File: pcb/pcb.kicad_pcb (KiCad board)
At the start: 2 copper layers, 168.9 x 103.7 mm, 129 parts, among them J1 MJ-4PP-9, J2 MJ-4PP-9, J3 USB_C_Receptacle_USB2.0_16P, J4 USB to TTL, J5 Conn_01x03, J6 Conn_01x03, SW1 KEY_SW, SW10 KEY_SW, SW11 KEY_SW, SW12 KEY_SW, SW13 KEY_SW, SW14 KEY_SW, SW15 KEY_SW, SW16 KEY_SW, SW17 KEY_SW, SW18 KEY_SW, SW19 KEY_SW, SW2 KEY_SW, SW20 KEY_SW, SW21 KEY_SW, SW22 KEY_SW, SW23 KEY_SW, SW24 KEY_SW, SW25 KEY_SW, SW26 KEY_SW, SW27 RotaryEncoder, SW3 KEY_SW, SW30 KEY_SW, SW31 KEY_SW, SW32 KEY_SW, SW33 KEY_SW, SW34 KEY_SW, SW35 KEY_SW, SW36 KEY_SW, SW37 KEY_SW, SW38 KEY_SW, SW39 KEY_SW, SW4 KEY_SW, SW40 KEY_SW, SW41 KEY_SW, SW42 KEY_SW, SW43 KEY_SW, SW44 KEY_SW, SW45 KEY_SW, SW46 KEY_SW, SW47 KEY_SW, SW48 KEY_SW, SW49 KEY_SW, SW5 KEY_SW, SW50 KEY_SW, SW51 KEY_SW, SW52 KEY_SW, SW53 KEY_SW, SW54 KEY_SW, SW6 KEY_SW, SW60 RESET_SW, SW61 BOOT_SW, SW7 KEY_SW, SW8 KEY_SW, SW9 KEY_SW, SW６２1 DIP_SW, U1 ESP32-S3-WROOM-1, U2 TPS1117LV33S, U3 USBLC6-2SC6

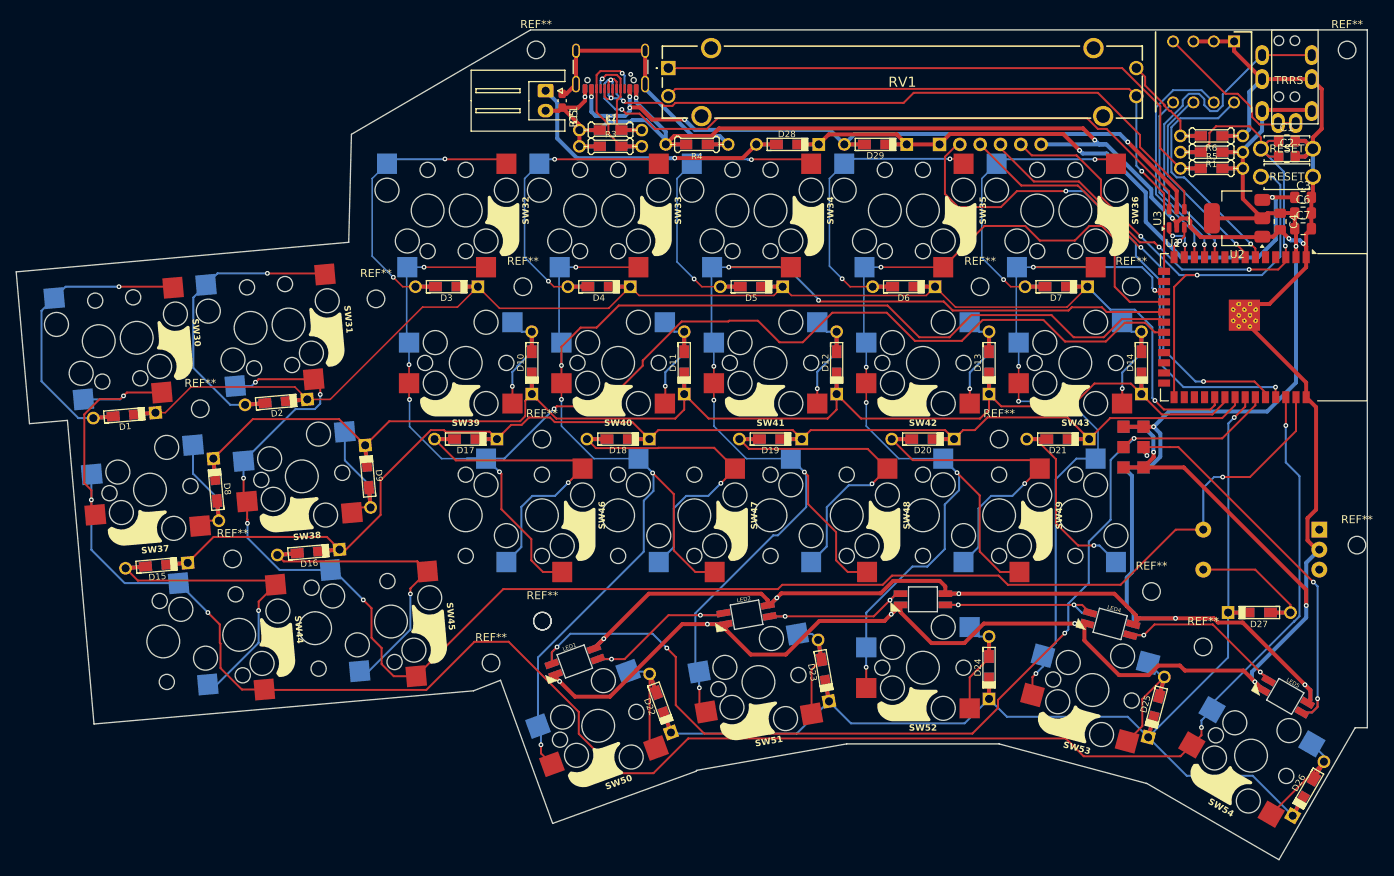
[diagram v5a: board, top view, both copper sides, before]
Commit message: put M2 hole
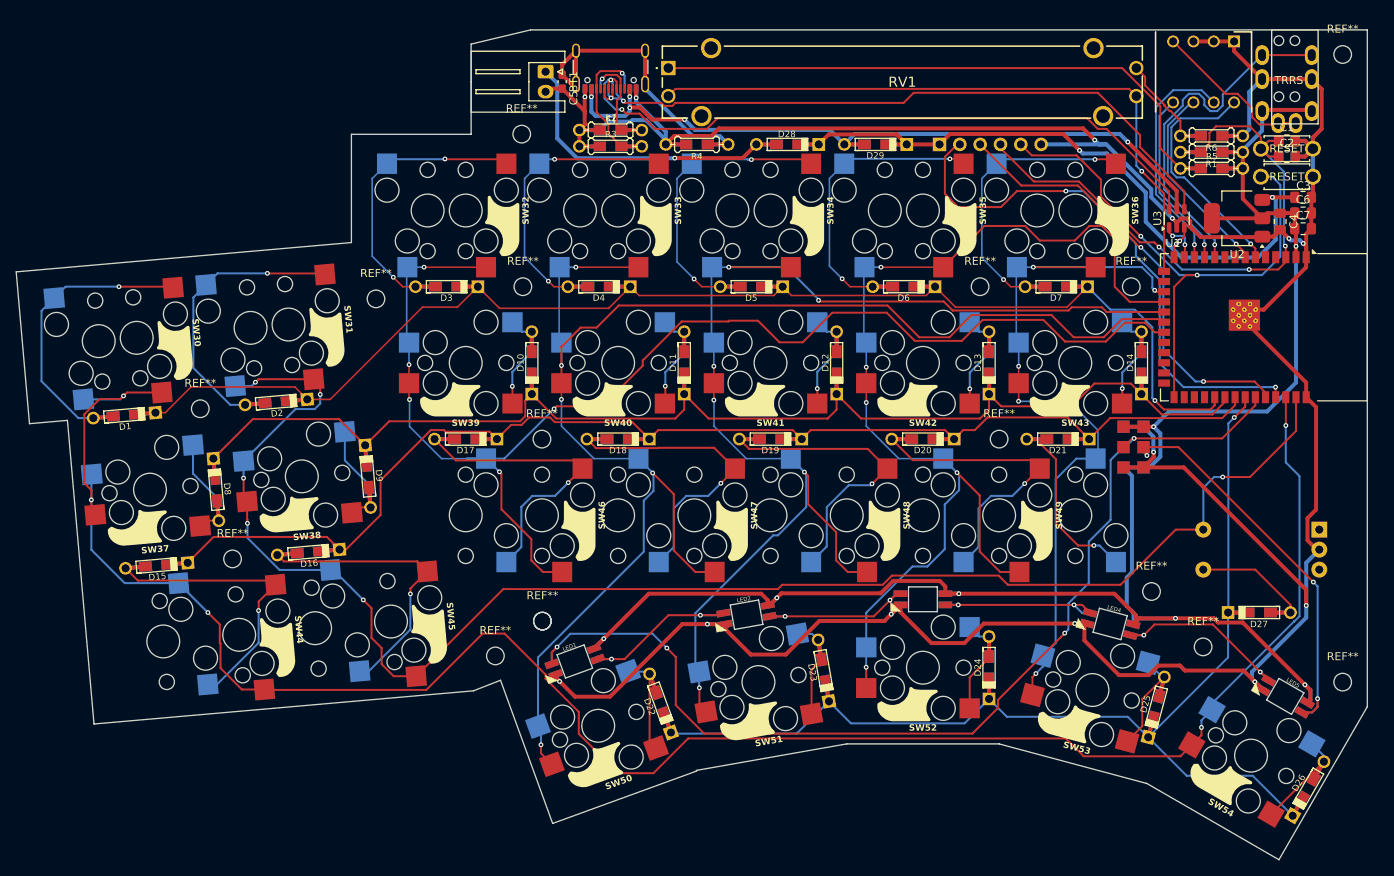
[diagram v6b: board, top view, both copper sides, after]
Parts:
- BT1: footprint Connector_JST:JST_XH_S2B-XH-A_1x02_P2.50mm_Horizontal -> lib:JST_XH_S2B-XH-A_1x02_P2.50mm_Horizontal
- J4: footprint Connector_PinSocket_2.54mm:PinSocket_1x06_P2.54mm_Horizontal -> lib:PinSocket_1x06_P2.54mm_Horizontal
- moved REF** 17.2 mm to (203.2, 124.6)
- moved REF** 10.7 mm to (100.6, 56.1)
- moved BT1 2.38 mm to (103.6, 48.3)
- moved C5 2.37 mm to (105.6, 49.6)
- moved REF** 1.04 mm to (97.3, 121.4)
- moved REF** 0.79 mm to (203.2, 46.2)
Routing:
- net Net-(J3-SHIELD): track 33.7 -> 37.4 mm
- net Net-(BT1-+): track 33.2 -> 35.6 mm
- net col0: track 250.5 -> 251.7 mm
- net GND: track 412.0 -> 412.9 mm
- net (no net): vias 1 -> 0
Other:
- outline, holes or cut-outs redrawn

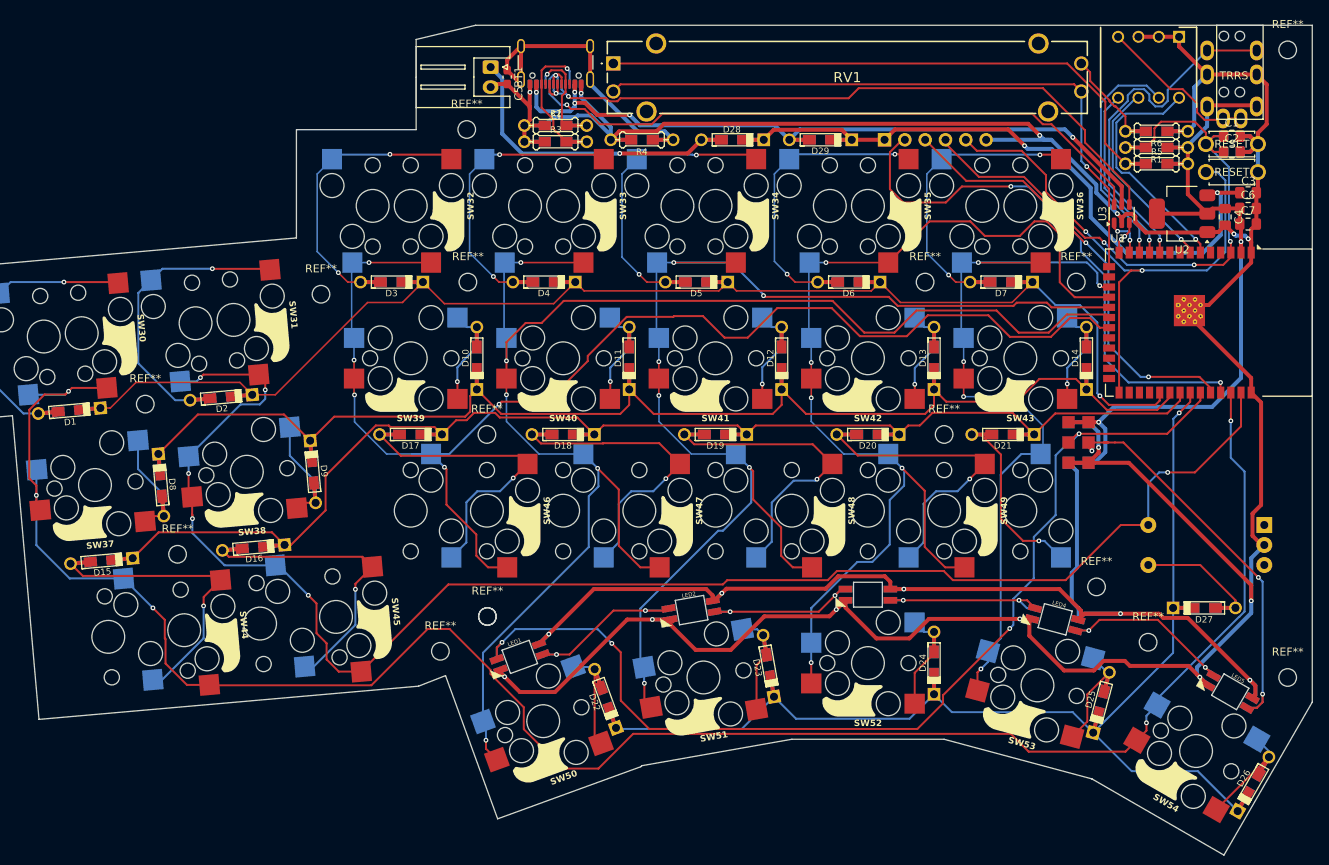
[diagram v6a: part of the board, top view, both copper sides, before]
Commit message: completed DRC
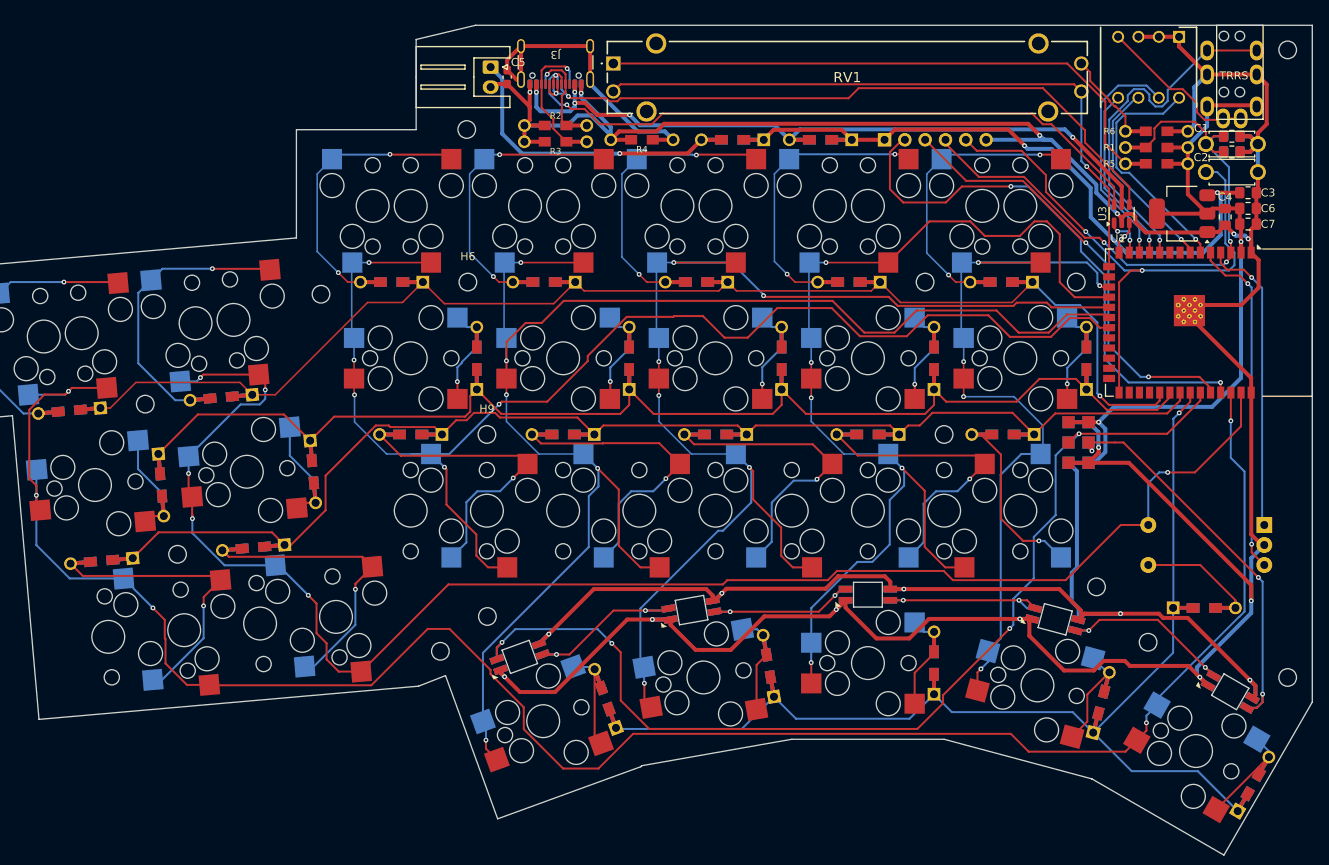
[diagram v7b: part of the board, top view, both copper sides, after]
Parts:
- removed ?: , 
- D1, D10, D11, D12, D13, D14, D15, D16, D17, D18, D19, D2, D20, D21, D22, D23, D24, D25, D26, D27, D28, D29, D3, D4, D5, D6, D7, D8, D9: footprint keebio:Diode-dual -> lib:Diode-dual
- R1, R2, R3, R4, R5, R6: footprint keebio:Resistor-Hybrid -> lib:Resistor-Hybrid
- SW1, SW15, SW16, SW17, SW18, SW19, SW2, SW20, SW21, SW3, SW30, SW31, SW32, SW33, SW34, SW35, SW36, SW37, SW38, SW39, SW4, SW40, SW41, SW42, SW43, SW44, SW45, SW46, SW47, SW48, SW49, SW5, SW50, SW51, SW52, SW53, SW54, SW6, SW7: footprint kbd:keyswitch_cherrymx_hotswap_1u -> lib:keyswitch_cherrymx_hotswap_1u
- renumbered REF** to H1, REF** to H10, REF** to H11, REF** to H12, REF** to H13, REF** to H14, REF** to H15, REF** to H2, REF** to H3, REF** to H4, REF** to H5, REF** to H6, REF** to H7, REF** to H8, REF** to H9
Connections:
- U1 pad 4: unconnected-(U1-IO4-Pad4) -> rotaryA
- U1 pad 5: unconnected-(U1-IO5-Pad5) -> rotaryB
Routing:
- net rotaryB: track 0.00 -> 42.9 mm, vias 0 -> 2
- net rotaryA: track 0.00 -> 37.5 mm, vias 0 -> 1
- net GND: track 412.9 -> 417.7 mm
- net IO0: track 70.5 -> 73.1 mm
- net Net-(J5-Pin_2): track 52.6 -> 52.0 mm

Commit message: put logo
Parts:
- added REF**: logo, lib:logo, B.Cu at (195.9, 79.5)
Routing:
- net GND: track 417.7 -> 422.8 mm, vias 13 -> 39
- net rgb-led: track 131.1 -> 135.1 mm
- net Net-(J3-D+-PadA6): track 87.4 -> 90.6 mm
- net IO0: track 73.1 -> 76.3 mm
- net col1: track 198.4 -> 200.4 mm
- net Net-(U1-IO20): track 4.29 -> 5.63 mm
- net slider: track 82.6 -> 83.9 mm
- net EN: track 80.4 -> 81.5 mm
- net rotaryB: track 42.9 -> 44.0 mm
- net Net-(J3-D--PadA7): track 85.7 -> 86.8 mm
- net rotaryA: vias 1 -> 2
- added copper zone on B.Cu, net GND
- added copper zone on F.Cu, net GND
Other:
- board text added: "Voidaster Keyboard PCB Designed by K.S"
